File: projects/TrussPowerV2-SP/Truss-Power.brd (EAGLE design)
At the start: 40.3 x 20.3 mm, 20 parts, among them J1 XF2L-0535-1, U2 MCP73831T-2ACI/OT, U3 MAX17044, X1 22-23-2021, X2 MicroB, X3 22-23-2021

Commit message: Seeedstudio
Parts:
- removed CHRG: ORANGE, microbuilder:CHIPLED_0805_NOOUTLINE
- removed LED1: (no value), led:CHIP-LED0603
- removed R12: 4.7K, resistor:R0402
- removed U3: MAX17044, NewPart:TDFN
- added IC1: MAX17043X+T10, SamacSys_Parts:BGA9C40P3X3_160X142X69
- added LED3: APHB1608SYKSURKC, APHB1608SYKSURKC:APHB1608ZGSURKC
- moved R13 17.9 mm to (24.1, 18.9), turned to 0 degrees
- moved R7 5.57 mm to (31.4, 15.0), turned to 270 degrees
- moved R6 5.16 mm to (6.90, 14.1), turned to 0 degrees
- moved C5 5.07 mm to (8.19, 12.0), turned to 270 degrees
- moved R11 1.03 mm to (6.87, 15.4), turned to 0 degrees
- moved C11 0.72 mm to (10.8, 15.0)
- moved C3 0.18 mm to (33.9, 18.9)
- moved X1 0.09 mm to (3.05, 3.76), turned to 180 degrees
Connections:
- removed net ALRT: J1.2, R12.2, U3.5
- net GND: now also IC1.A3, IC1.B1, IC1.C3, LED3.4; no longer R13.1, U3.1, U3.4, U3.6, U3.9
- net LEDSOC: now also R13.2; no longer LED1.A
- net N$1: now also IC1.B3; no longer U3.2
- net N$3: now also IC1.C2; no longer U3.3
- net N$4: now also LED3.1, R7.1; no longer LED1.C, R13.2
- net N$5: now also LED3.2, U2.1; no longer CHRG.A, R7.1
- net N$6: now also LED3.3, R13.1; no longer CHRG.C, U2.1
- net SCL: now also IC1.A2; no longer U3.7
- net SDA: now also IC1.A1; no longer U3.8
- net VBAT: no longer R12.1
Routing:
- net LEDSOC: track 6.32 -> 23.7 mm
- net ALRT: track 8.52 -> 0.00 mm, vias 1 -> 0
- net N$6: track 0.00 -> 8.47 mm
- net GND: track 19.8 -> 13.8 mm, vias 7 -> 5
- net N$5: track 0.00 -> 3.03 mm, vias 0 -> 1
- net N$1: track 5.55 -> 2.92 mm
- net N$4: track 4.78 -> 3.54 mm, vias 0 -> 1
- net SCL: track 16.3 -> 17.0 mm
- net SDA: track 14.8 -> 15.5 mm

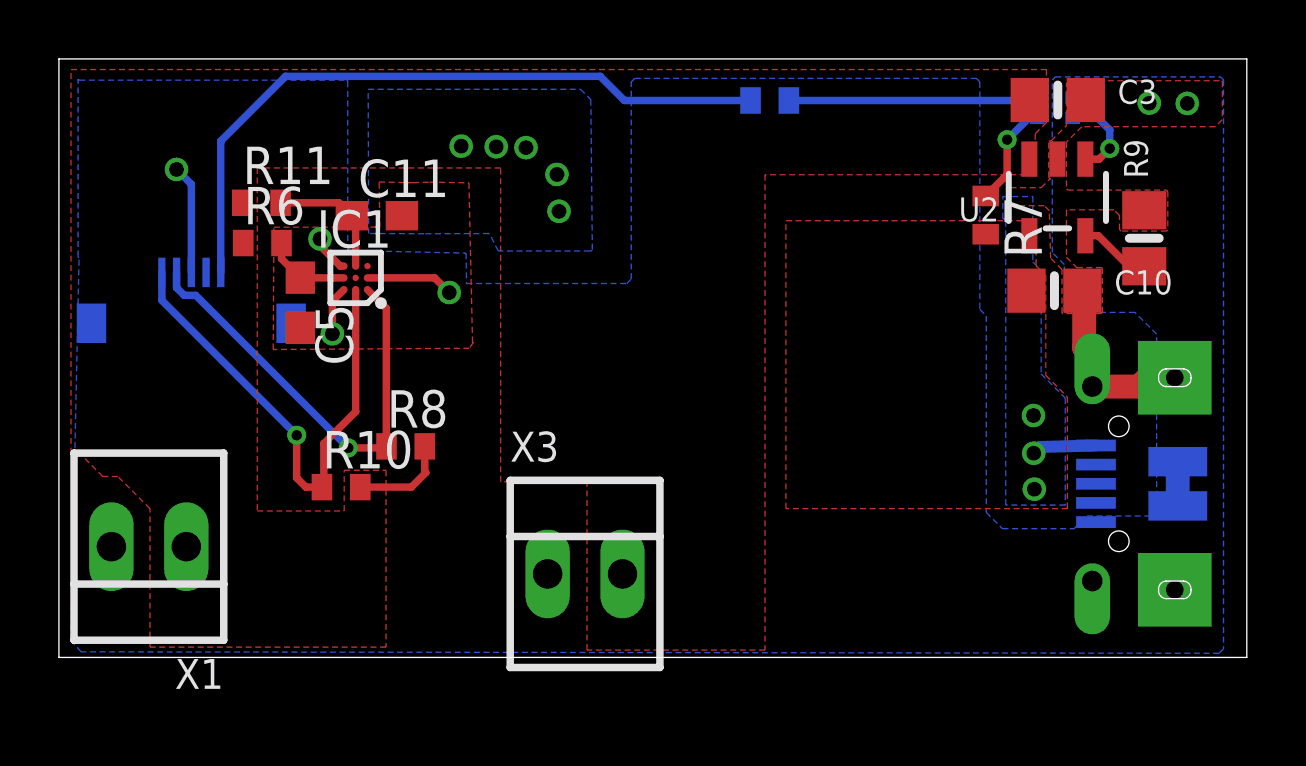
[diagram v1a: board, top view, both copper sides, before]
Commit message: Gas Gauge change
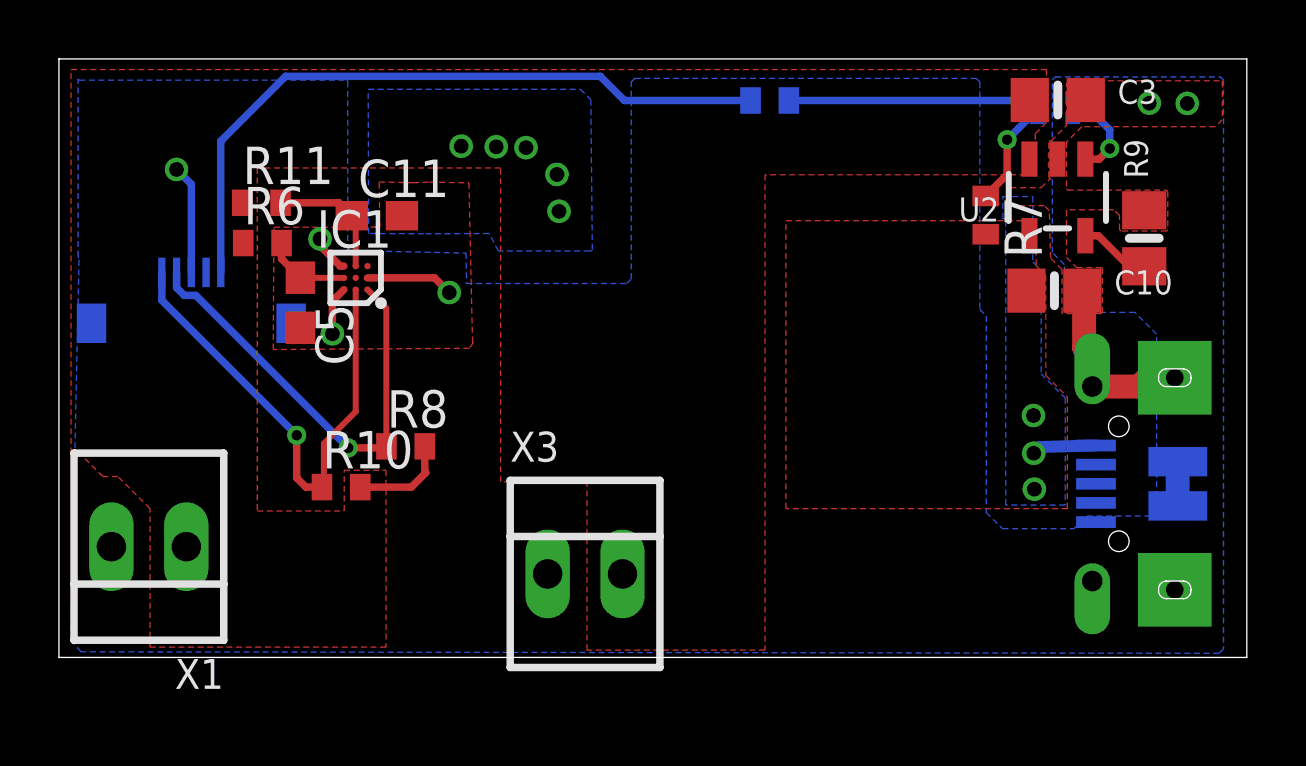
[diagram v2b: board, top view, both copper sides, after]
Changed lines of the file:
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@@
 <wire x1="3.4926" y1="12.1174" x2="8.07" y2="7.54" width="0.254" layer="16"/>
 <via x="8.07" y="7.54" extent="1-16" drill="0.35"/>
-<wire x1="8.99" y1="7.26" x2="8.99" y2="5.8442" width="0.254" layer="1"/>
 <wire x1="8.99" y1="5.8442" x2="8.926" y2="5.7802" width="0.254" layer="1"/>
 <wire x1="8.926" y1="5.7802" x2="8.3798" y2="5.7802" width="0.254" layer="1"/>
@@
 <wire x1="8.3798" y1="5.7802" x2="8.07" y2="6.09" width="0.254" layer="1"/>
 <contactref element="IC1" pad="A2"/>
-<wire x1="10.07" y1="8.34" x2="8.99" y2="7.26" width="0.254" layer="1"/>
-<wire x1="10.07" y1="12.48" x2="10.07" y2="8.34" width="0.254" layer="1"/>
+<wire x1="10.07" y1="12.48" x2="10.07" y2="8.34" width="0.2032" layer="1"/>
+<wire x1="10.07" y1="8.34" x2="8.99" y2="7.26" width="0.2032" layer="1"/>
+<wire x1="8.99" y1="7.26" x2="8.99" y2="5.8442" width="0.2032" layer="1"/>
 </signal>
 <signal name="SDA">
@@
 <via x="9.82" y="7.11" extent="1-16" drill="0.35"/>
 <wire x1="9.82" y1="7.11" x2="11.0624" y2="7.11" width="0.254" layer="1"/>
-<wire x1="11.11" y1="7.1576" x2="11.1152" y2="7.1628" width="0.254" layer="1"/>
 <wire x1="4.25186875" y1="12.2864" x2="4.6436" y2="12.2864" width="0.254" layer="16"/>
 <wire x1="3.9926" y1="13.0658" x2="3.9926" y2="12.54566875" width="0.254" layer="16"/>
@@
 <wire x1="4.6436" y1="12.2864" x2="9.82" y2="7.11" width="0.254" layer="16"/>
 <contactref element="IC1" pad="A1"/>
-<wire x1="11.11" y1="7.1576" x2="11.0624" y2="7.11" width="0.254" layer="1"/>
-<wire x1="11.11" y1="11.84" x2="11.11" y2="7.1576" width="0.254" layer="1"/>
-<wire x1="10.47" y1="12.48" x2="11.11" y2="11.84" width="0.254" layer="1"/>
+<wire x1="11.1152" y1="7.1628" x2="11.0624" y2="7.11" width="0.254" layer="1"/>
+<wire x1="10.47" y1="12.48" x2="11.11" y2="11.84" width="0.2032" layer="1"/>
+<wire x1="11.11" y1="11.84" x2="11.11" y2="7.168" width="0.2032" layer="1"/>
+<wire x1="11.11" y1="7.168" x2="11.1152" y2="7.1628" width="0.2032" layer="1"/>
 </signal>
 <signal name="N$2">
@@
 <wire x1="9.9386" y1="14.9886" x2="9.499" y2="15.4282" width="0.254" layer="1"/>
 <wire x1="9.499" y1="15.4282" x2="7.5216" y2="15.4282" width="0.254" layer="1"/>
-<wire x1="10.07" y1="13.28" x2="10.07" y2="14.8572" width="0.254" layer="1"/>
+<wire x1="10.07" y1="13.28" x2="10.07" y2="14.8572" width="0.2032" layer="1"/>
 </signal>
 <signal name="N$1">
@@
 <wire x1="7.5534" y1="14.062" x2="7.5534" y2="13.5262" width="0.254" layer="1"/>
 <wire x1="7.5534" y1="13.5262" x2="8.1934" y2="12.8862" width="0.254" layer="1"/>
-<wire x1="9.67" y1="12.88" x2="8.1996" y2="12.88" width="0.254" layer="1"/>
+<wire x1="9.67" y1="12.88" x2="8.1996" y2="12.88" width="0.2032" layer="1"/>
 </signal>
 <signal name="N$4">
